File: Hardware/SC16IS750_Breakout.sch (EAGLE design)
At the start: 17 parts, among them IC1 SC16IS750, Q1 14.7456MHz, U1 3.3V

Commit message: Fixed board files
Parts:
- C1, C2, C4: device SparkFun:CAP0402-CAP -> SparkFun-Passives:CAP0603-CAP
- IC1: device SparkFun:SC16IS750 -> SparkFun-DigitalIC:SC16IS750
- R1, R2, R3: device SparkFun:RESISTOR0402-RES -> SparkFun-Passives:RESISTOR0603-RES
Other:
- note added: "C. Taylor, Updated by: T. Klopfenstein"
- note removed: "Chris Taylor"

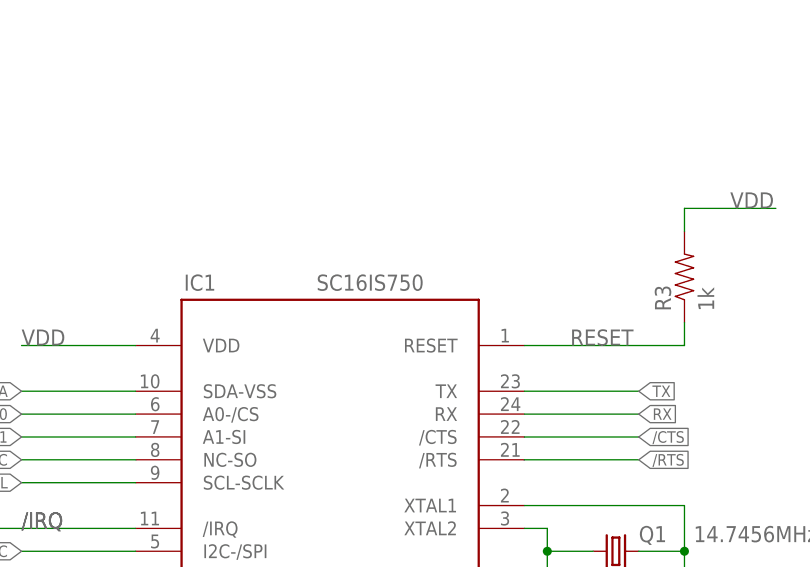
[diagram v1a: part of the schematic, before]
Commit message: Updated Package to "1:1" and rerouted traces directly away from IC
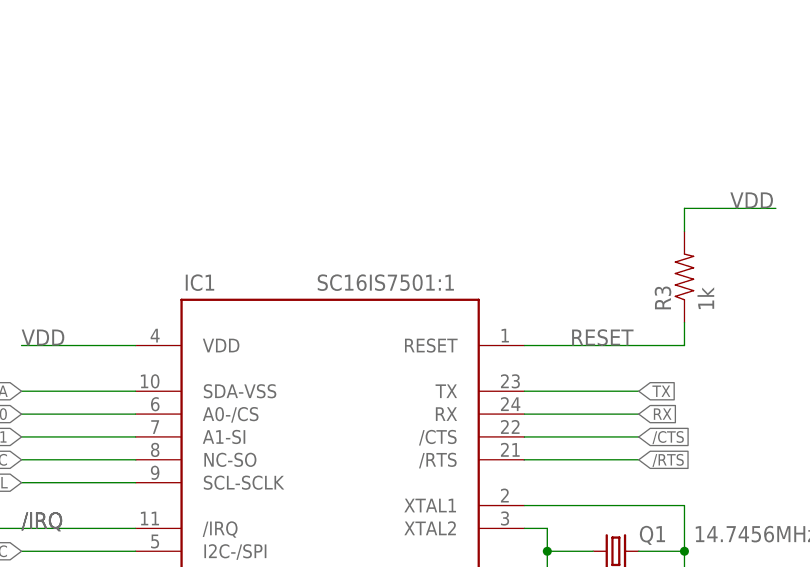
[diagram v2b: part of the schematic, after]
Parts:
- IC1: value SC16IS750 -> SC16IS7501:1; device SparkFun-DigitalIC:SC16IS750 -> Testing:SC16IS7501:1
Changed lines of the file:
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@@
 <grid distance="0.1" unitdist="inch" unit="inch" style="lines" multiple="1" display="no" altdistance="0.01" altunitdist="inch" altunit="inch"/>
 <layers>
-<layer number="1" name="Top" color="4" fill="1" visible="yes" active="no"/>
-<layer number="2" name="Route2" color="1" fill="3" visible="yes" active="no"/>
-<layer number="3" name="Route3" color="4" fill="3" visible="yes" active="no"/>
-<layer number="4" name="Route4" color="1" fill="4" visible="yes" active="no"/>
-<layer number="5" name="Route5" color="4" fill="4" visible="yes" active="no"/>
-<layer number="6" name="Route6" color="1" fill="8" visible="yes" active="no"/>
-<layer number="7" name="Route7" color="4" fill="8" visible="yes" active="no"/>
-<layer number="8" name="Route8" color="1" fill="2" visible="yes" active="no"/>
-<layer number="9" name="Route9" color="4" fill="2" visible="yes" active="no"/>
-<layer number="10" name="Route10" color="1" fill="7" visible="yes" active="no"/>
-<layer number="11" name="Route11" color="4" fill="7" visible="yes" active="no"/>
-<layer number="12" name="Route12" color="1" fill="5" visible="yes" active="no"/>
-<layer number="13" name="Route13" color="4" fill="5" visible="yes" active="no"/>
-<layer number="14" name="Route14" color="1" fill="6" visible="yes" active="no"/>
-<layer number="15" name="Route15" color="4" fill="6" visible="yes" active="no"/>
-<layer number="16" name="Bottom" color="1" fill="1" visible="yes" active="no"/>
-<layer number="17" name="Pads" color="2" fill="1" visible="yes" active="no"/>
-<layer number="18" name="Vias" color="2" fill="1" visible="yes" active="no"/>
-<layer number="19" name="Unrouted" color="6" fill="1" visible="yes" active="no"/>
-<layer number="20" name="Dimension" color="15" fill="1" visible="yes" active="no"/>
-<layer number="21" name="tPlace" color="16" fill="1" visible="yes" active="no"/>
-<layer number="22" name="bPlace" color="14" fill="1" visible="yes" active="no"/>
-<layer number="23" name="tOrigins" color="15" fill="1" visible="yes" active="no"/>
-<layer number="24" name="bOrigins" color="15" fill="1" visible="yes" active="no"/>
-<layer number="25" name="tNames" color="7" fill="1" visible="yes" active="no"/>
-<layer number="26" name="bNames" color="7" fill="1" visible="yes" active="no"/>
-<layer number="27" name="tValues" color="7" fill="1" visible="yes" active="no"/>
-<layer number="28" name="bValues" color="7" fill="1" visible="yes" active="no"/>
+<layer number="1" name="Top" color="4" fill="1" visible="no" active="no"/>
+<layer number="2" name="Route2" color="1" fill="3" visible="no" active="no"/>
+<layer number="3" name="Route3" color="4" fill="3" visible="no" active="no"/>
+<layer number="4" name="Route4" color="1" fill="4" visible="no" active="no"/>
+<layer number="5" name="Route5" color="4" fill="4" visible="no" active="no"/>
+<layer number="6" name="Route6" color="1" fill="8" visible="no" active="no"/>
+<layer number="7" name="Route7" color="4" fill="8" visible="no" active="no"/>
+<layer number="8" name="Route8" color="1" fill="2" visible="no" active="no"/>
+<layer number="9" name="Route9" color="4" fill="2" visible="no" active="no"/>
+<layer number="10" name="Route10" color="1" fill="7" visible="no" active="no"/>
+<layer number="11" name="Route11" color="4" fill="7" visible="no" active="no"/>
+<layer number="12" name="Route12" color="1" fill="5" visible="no" active="no"/>
+<layer number="13" name="Route13" color="4" fill="5" visible="no" active="no"/>
+<layer number="14" name="Route14" color="1" fill="6" visible="no" active="no"/>
+<layer number="15" name="Route15" color="4" fill="6" visible="no" active="no"/>
+<layer number="16" name="Bottom" color="1" fill="1" visible="no" active="no"/>
+<layer number="17" name="Pads" color="2" fill="1" visible="no" active="no"/>
+<layer number="18" name="Vias" color="2" fill="1" visible="no" active="no"/>
+<layer number="19" name="Unrouted" color="6" fill="1" visible="no" active="no"/>
+<layer number="20" name="Dimension" color="15" fill="1" visible="no" active="no"/>
+<layer number="21" name="tPlace" color="16" fill="1" visible="no" active="no"/>
+<layer number="22" name="bPlace" color="14" fill="1" visible="no" active="no"/>
+<layer number="23" name="tOrigins" color="15" fill="1" visible="no" active="no"/>
+<layer number="24" name="bOrigins" color="15" fill="1" visible="no" active="no"/>
+<layer number="25" name="tNames" color="7" fill="1" visible="no" active="no"/>
+<layer number="26" name="bNames" color="7" fill="1" visible="no" active="no"/>
+<layer number="27" name="tValues" color="7" fill="1" visible="no" active="no"/>
+<layer number="28" name="bValues" color="7" fill="1" visible="no" active="no"/>
 <layer number="29" name="tStop" color="7" fill="3" visible="no" active="no"/>
 <layer number="30" name="bStop" color="7" fill="6" visible="no" active="no"/>
@@
 <layer number="35" name="tGlue" color="7" fill="4" visible="no" active="no"/>
 <layer number="36" name="bGlue" color="7" fill="5" visible="no" active="no"/>
-<layer number="37" name="tTest" color="7" fill="1" visible="yes" active="no"/>
-<layer number="38" name="bTest" color="7" fill="1" visible="yes" active="no"/>
+<layer number="37" name="tTest" color="7" fill="1" visible="no" active="no"/>
+<layer number="38" name="bTest" color="7" fill="1" visible="no" active="no"/>
 <layer number="39" name="tKeepout" color="4" fill="11" visible="no" active="no"/>
 <layer number="40" name="bKeepout" color="1" fill="11" visible="no" active="no"/>
@@
 <layer number="44" name="Drills" color="7" fill="1" visible="no" active="no"/>
 <layer number="45" name="Holes" color="7" fill="1" visible="no" active="no"/>
-<layer number="46" name="Milling" color="3" fill="1" visible="yes" active="no"/>
-<layer number="47" name="Measures" color="7" fill="1" visible="yes" active="no"/>
-<layer number="48" name="Document" color="7" fill="1" visible="yes" active="no"/>
-<layer number="49" name="Reference" color="7" fill="1" visible="yes" active="no"/>
-<layer number="50" name="dxf" color="7" fill="1" visible="yes" active="no"/>
-<layer number="51" name="tDocu" color="6" fill="1" visible="yes" active="no"/>
-<layer number="52" name="bDocu" color="7" fill="1" visible="yes" active="no"/>
-<layer number="53" name="tGND_GNDA" color="7" fill="9" visible="yes" active="no"/>
-<layer number="54" name="bGND_GNDA" color="1" fill="9" visible="yes" active="no"/>
-<layer number="56" name="wert" color="7" fill="1" visible="yes" active="no"/>
+<layer number="46" name="Milling" color="3" fill="1" visible="no" active="no"/>
+<layer number="47" name="Measures" color="7" fill="1" visible="no" active="no"/>
+<layer number="48" name="Document" color="7" fill="1" visible="no" active="no"/>
+<layer number="49" name="Reference" color="7" fill="1" visible="no" active="no"/>
+<layer number="50" name="dxf" color="7" fill="1" visible="no" active="no"/>
+<layer number="51" name="tDocu" color="6" fill="1" visible="no" active="no"/>
+<layer number="52" name="bDocu" color="7" fill="1" visible="no" active="no"/>
+<layer number="53" name="tGND_GNDA" color="7" fill="9" visible="no" active="no"/>
+<layer number="54" name="bGND_GNDA" color="1" fill="9" visible="no" active="no"/>
+<layer number="56" name="wert" color="7" fill="1" visible="no" active="no"/>
 <layer number="91" name="Nets" color="2" fill="1" visible="yes" active="yes"/>
 <layer number="92" name="Busses" color="1" fill="1" visible="yes" active="yes"/>
@@
 <layer number="106" name="bPlate" color="7" fill="1" visible="yes" active="yes"/>
 <layer number="107" name="Crop" color="7" fill="1" visible="yes" active="yes"/>
+<layer number="108" name="tplace-old" color="10" fill="1" visible="yes" active="yes"/>
+<layer number="109" name="ref-old" color="11" fill="1" visible="yes" active="yes"/>
 <layer number="116" name="Patch_BOT" color="9" fill="4" visible="yes" active="yes"/>
 <layer number="121" name="_tsilk" color="7" fill="1" visible="yes" active="yes"/>
@@
 <layer number="144" name="Drill_legend" color="7" fill="1" visible="no" active="yes"/>
 <layer number="151" name="HeatSink" color="7" fill="1" visible="yes" active="yes"/>
+<layer number="199" name="Contour" color="7" fill="1" visible="yes" active="yes"/>
 <layer number="200" name="200bmp" color="1" fill="10" visible="yes" active="yes"/>
 <layer number="201" name="201bmp" color="2" fill="10" visible="yes" active="yes"/>
@@
 </classes>
 <parts>
-<part name="IC1" library="SparkFun-DigitalIC" deviceset="SC16IS750" device=""/>
+<part name="IC1" library="Testing" deviceset="SC16IS750" device="1:1"/>
 <part name="Q1" library="SparkFun" deviceset="CRYSTAL" device="5X3" value="14.7456MHz"/>
 <part name="C1" library="SparkFun-Passives" deviceset="CAP" device="0603-CAP" value="18pF"/>
